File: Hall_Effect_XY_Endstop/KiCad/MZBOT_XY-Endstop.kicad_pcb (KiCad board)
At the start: 2 copper layers, 56 x 18 mm, 26 parts, among them J1 CONN_01X04, U1 SS49E, U2 SS49E, U3 LM393, U4 AP2210N

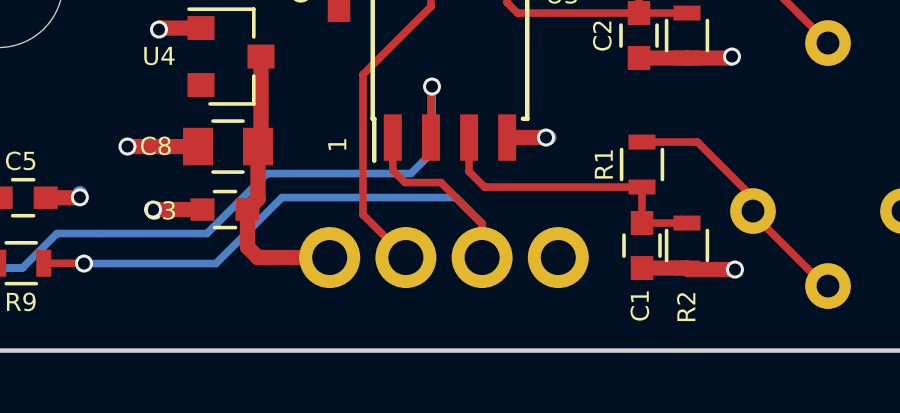
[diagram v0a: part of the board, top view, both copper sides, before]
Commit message: Gerbers and Silkscreen update
Added Silkscreen label to the 4-pin connector
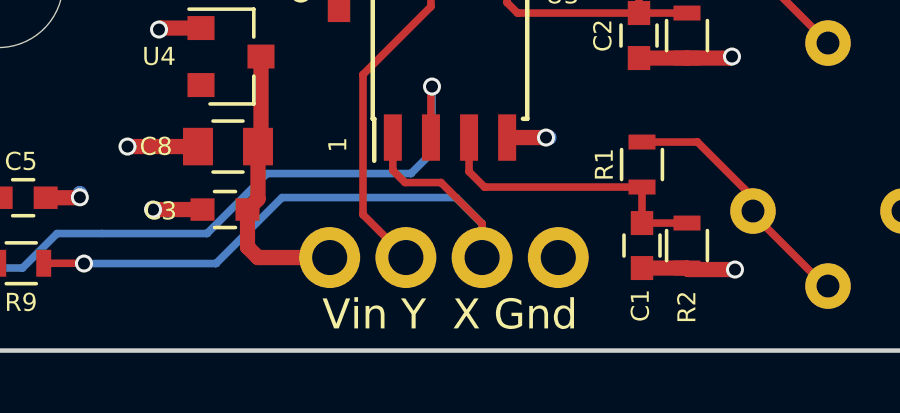
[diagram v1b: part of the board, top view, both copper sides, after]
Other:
- board text added: "Gnd X Y Vin"
- board text added: "Vin Y X Gnd"
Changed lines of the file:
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@@
-(kicad_pcb (version 20171130) (host pcbnew "(5.0.0-3-g5ebb6b6)")
+(kicad_pcb (version 20171130) (host pcbnew "(5.1.5)-3")
   (general
     (thickness 1.6)
-    (drawings 28)
+    (drawings 30)
     (tracks 121)
     (zones 0)
@@
   (layers
     (0 F.Cu signal)
-    (31 B.Cu signal hide)
+    (31 B.Cu signal)
     (32 B.Adhes user)
     (33 F.Adhes user)
     (34 B.Paste user)
-    (35 F.Paste user hide)
+    (35 F.Paste user)
     (36 B.SilkS user)
     (37 F.SilkS user)
@@
     (zone_45_only no)
     (trace_min 0.2)
-    (segment_width 0.2)
-    (edge_width 0.15)
     (via_size 0.6)
     (via_drill 0.4)
@@
     (uvia_min_size 0.2)
     (uvia_min_drill 0.1)
+    (edge_width 0.15)
+    (segment_width 0.2)
     (pcb_text_width 0.3)
     (pcb_text_size 1.5 1.5)
@@
     (pad_to_mask_clearance 0.2)
     (aux_axis_origin 0 0)
-    (visible_elements 7FFEFFFF)
+    (visible_elements 7FFFFFFF)
     (pcbplotparams
       (layerselection 0x010f0_ffffffff)
@@
       (xy 0.011887 1.460649)) (layer B.SilkS) (width 0.01))
   )
+  (gr_text "Gnd X  Y Vin" (at 142.8 109.8) (layer B.SilkS)
+    (effects (font (size 1 1) (thickness 0.15)) (justify mirror))
+  )
+  (gr_text "Vin Y  X Gnd" (at 142.8 109.8) (layer F.SilkS)
+    (effects (font (size 1 1) (thickness 0.15)))
+  )
   (gr_text 1 (at 139.065 104.14 90) (layer F.SilkS)
